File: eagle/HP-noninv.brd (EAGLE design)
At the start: 40.7 x 40.7 mm, 20 parts, among them IC1 OPA2134, IC2 TLE2426CLP

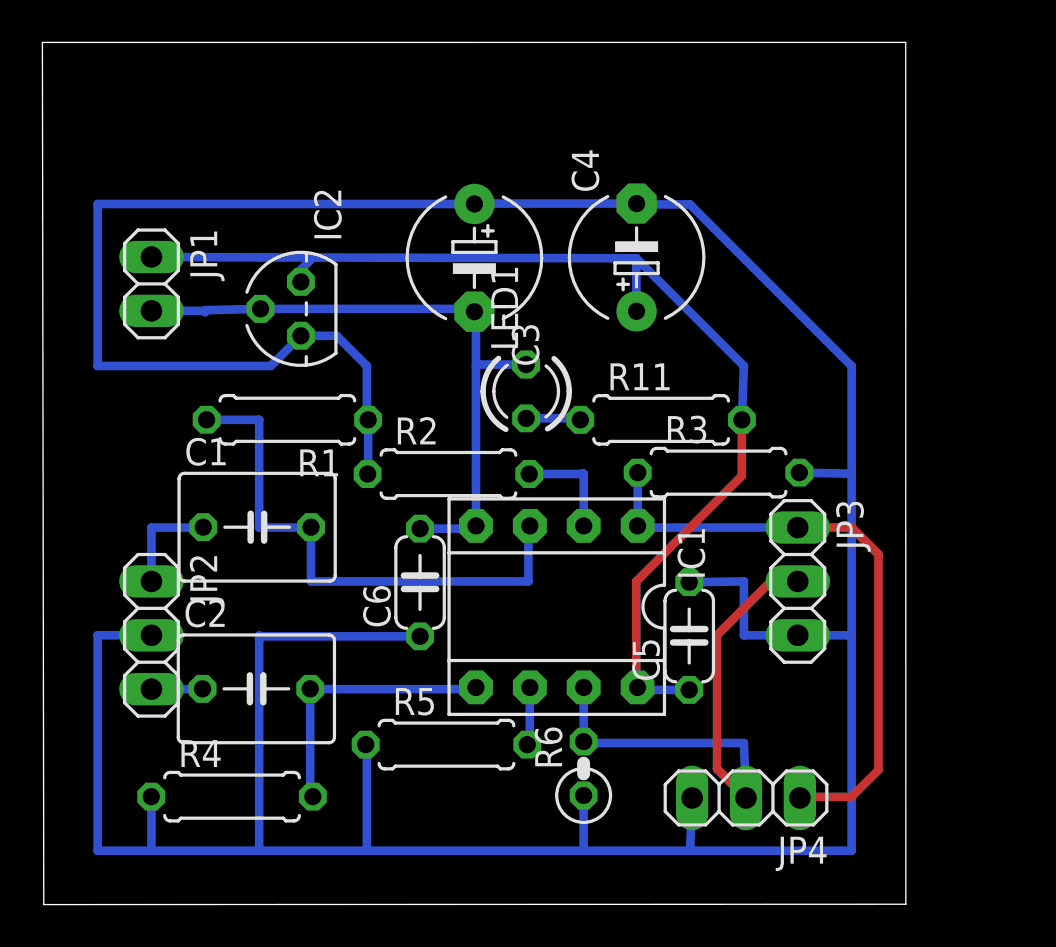
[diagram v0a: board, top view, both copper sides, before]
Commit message: 保護抵抗追加
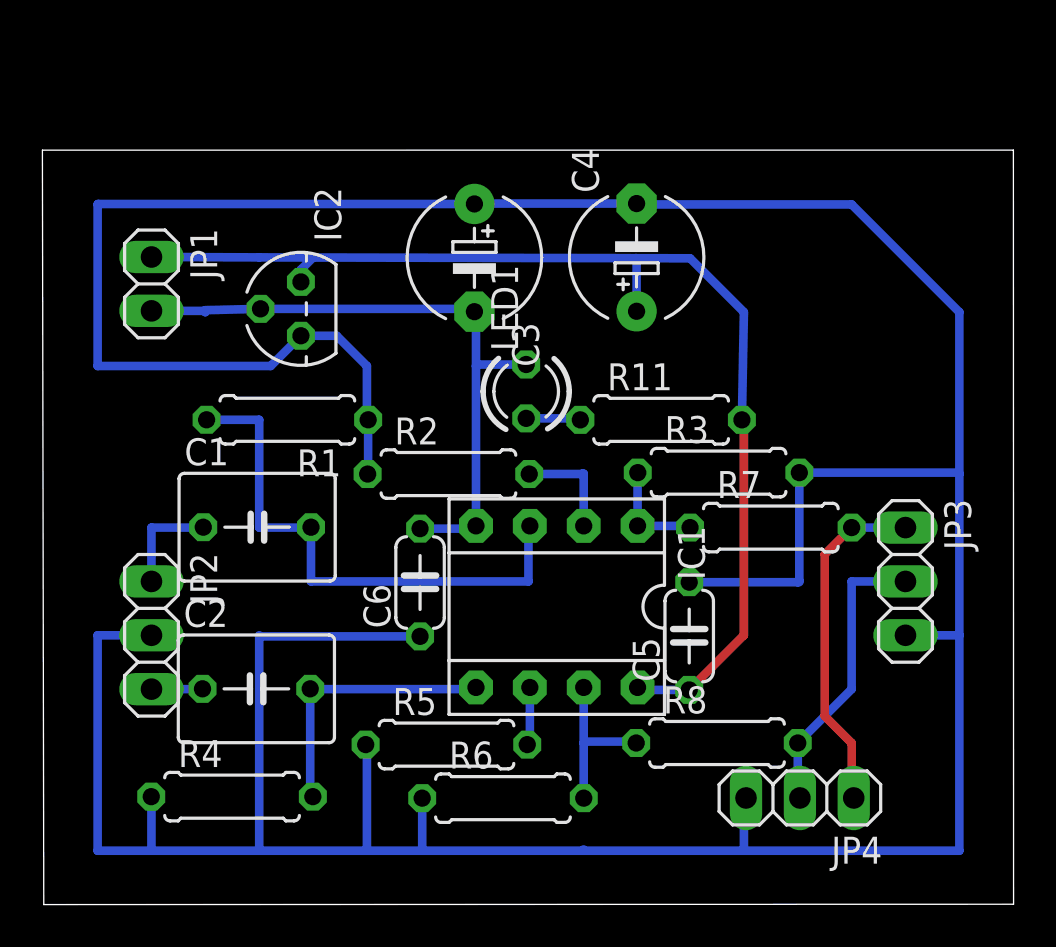
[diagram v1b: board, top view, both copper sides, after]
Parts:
- added R7, R8: (no value), rcl:0207/7
- R6: device rcl:0207/2V -> rcl:0207/7
- moved JP3 5.08 mm to (40.6, 15.2)
- moved R6 4.05 mm to (21.7, 5.02), turned to 0 degrees
- moved JP4 2.54 mm to (35.7, 5.03)
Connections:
- new net N$2: IC1.1, R3.1, R7.1
- new net N$4: IC1.7, R6.2, R8.1
- net N$11: now also R8.2; no longer IC1.7, R6.2
- net N$8: now also R7.2; no longer IC1.1, R3.1
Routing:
- net GND: track 179.7 -> 199.2 mm
- net N$8: track 28.9 -> 16.4 mm
- net N$11: track 26.0 -> 13.9 mm
- net N$4: track 0.00 -> 7.75 mm
- net N$2: track 0.00 -> 5.08 mm
- net VCC: track 53.7 -> 54.4 mm
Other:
- board size 40.7 x 40.7 mm -> 45.8 x 35.6 mm

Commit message: ケミコンを倒して配置
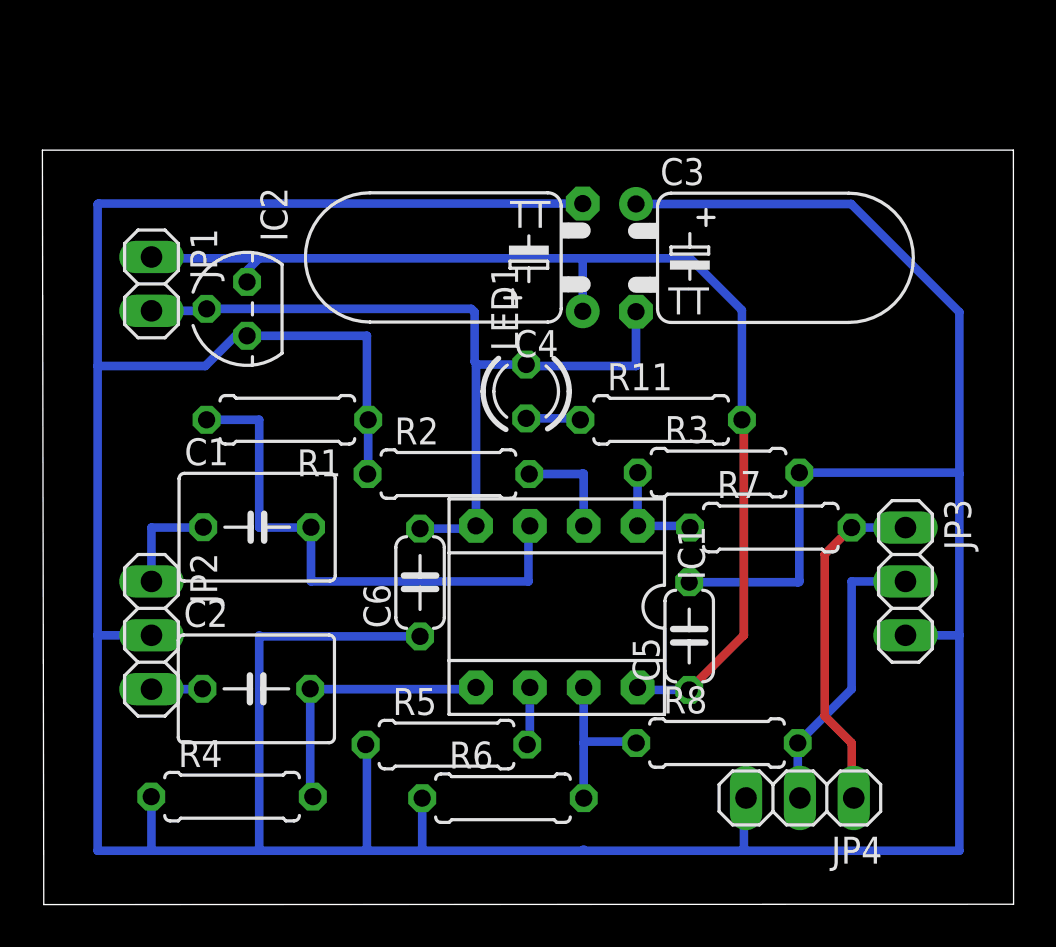
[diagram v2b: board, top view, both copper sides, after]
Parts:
- C3, C4: device rcl:E5-6 -> rcl:TT5D6L
- R11: value 1k -> 4.7k
- R7, R8: value (none) -> 22
- moved C3 7.62 mm to (27.9, 30.5)
- moved C4 2.54 mm to (25.4, 30.5)
- moved IC2 2.54 mm to (9.59, 28.1)
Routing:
- net GND: track 199.2 -> 210.2 mm
- net VEE: track 30.7 -> 38.5 mm
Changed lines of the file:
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@@
 <element name="R6" library="rcl" package="0207/7" value="47k" x="21.6567" y="5.019375"/>
 <element name="JP1" library="pinhead" package="1X02" value="PWR" x="5.080871875" y="29.271534375" rot="R270"/>
-<element name="R11" library="rcl" package="0207/7" value="1k" x="29.115325" y="22.860184375"/>
+<element name="R11" library="rcl" package="0207/7" value="4.7k" x="29.115325" y="22.860184375"/>
 <element name="LED1" library="led" package="LED3MM" value="Blue" x="22.75166875" y="24.200390625" rot="R90"/>
-<element name="IC2" library="tle2426" package="TO226AA" value="TLE2426CLP" x="12.1279375" y="28.09585" rot="R90"/>
-<element name="C3" library="rcl" package="E5-6" value="100u" x="20.310715625" y="30.502884375" rot="R270"/>
-<element name="C4" library="rcl" package="E5-6" value="100u" x="27.95845" y="30.520903125" rot="R90"/>
+<element name="IC2" library="tle2426" package="TO226AA" value="TLE2426CLP" x="9.5879375" y="28.09585" rot="R90"/>
+<element name="C3" library="rcl" package="TT5D6L" value="100u" x="27.930715625" y="30.502884375" rot="R270"/>
+<element name="C4" library="rcl" package="TT5D6L" value="100u" x="25.41845" y="30.520903125" rot="R90"/>
 <element name="C5" library="rcl" package="C050-024X044" value="0.1u" x="30.440721875" y="12.664484375" rot="R90"/>
 <element name="C6" library="rcl" package="C050-024X044" value="0.1u" x="17.74674375" y="15.189546875" rot="R90"/>
@@
 <element name="JP3" library="pinhead" package="1X03" value="OUTPUT1" x="40.64" y="15.24" rot="R270"/>
 <element name="JP4" library="pinhead" package="1X03" value="OUTPUT2" x="35.66021875" y="5.0287125" rot="R180"/>
-<element name="R7" library="rcl" package="0207/7" value="" x="34.29" y="17.78"/>
-<element name="R8" library="rcl" package="0207/7" value="" x="31.75" y="7.62"/>
+<element name="R7" library="rcl" package="0207/7" value="22" x="34.29" y="17.78"/>
+<element name="R8" library="rcl" package="0207/7" value="22" x="31.75" y="7.62"/>
 </elements>
 <signals>
@@
 <wire x1="15.182175" y1="7.54454375" x2="15.24" y2="7.54454375" width="0.4064" layer="16"/>
 <wire x1="15.24" y1="7.54454375" x2="15.24" y2="2.54" width="0.4064" layer="16"/>
-<wire x1="13.81415" y1="26.82585" x2="15.24" y2="25.4" width="0.4064" layer="16"/>
-<wire x1="15.24" y1="25.4" x2="15.24" y2="22.92230625" width="0.4064" layer="16"/>
+<wire x1="15.24" y1="26.82585" x2="15.24" y2="22.92230625" width="0.4064" layer="16"/>
 <wire x1="15.24" y1="22.92230625" x2="15.298746875" y2="22.863559375" width="0.4064" layer="16"/>
 <wire x1="15.298746875" y1="22.863559375" x2="15.298746875" y2="20.328196875" width="0.4064" layer="16"/>
 <wire x1="15.298746875" y1="20.328196875" x2="15.2750875" y2="20.3045375" width="0.4064" layer="16"/>
-<wire x1="27.95845" y1="33.060903125" x2="20.328734375" y2="33.060903125" width="0.4064" layer="16"/>
-<wire x1="20.328734375" y1="33.060903125" x2="20.310715625" y2="33.042884375" width="0.4064" layer="16"/>
 <contactref element="JP2" pad="2"/>
 <wire x1="5.08" y1="12.7" x2="2.54" y2="12.7" width="0.4064" layer="16"/>
 <wire x1="2.54" y1="12.7" x2="2.54" y2="2.54" width="0.4064" layer="16"/>
 <wire x1="2.54" y1="2.54" x2="5.08" y2="2.54" width="0.4064" layer="16"/>
-<wire x1="12.1279375" y1="26.82585" x2="10.7020875" y2="25.4" width="0.4064" layer="16"/>
-<wire x1="10.7020875" y1="25.4" x2="2.54" y2="25.4" width="0.4064" layer="16"/>
-<wire x1="2.54" y1="25.4" x2="2.54" y2="33.02" width="0.4064" layer="16"/>
-<wire x1="2.54" y1="33.02" x2="2.562884375" y2="33.042884375" width="0.4064" layer="16"/>
-<wire x1="2.562884375" y1="33.042884375" x2="20.310715625" y2="33.042884375" width="0.4064" layer="16"/>
-<wire x1="12.1279375" y1="26.82585" x2="13.81415" y2="26.82585" width="0.4064" layer="16"/>
+<wire x1="2.54" y1="33.02" x2="2.580903125" y2="33.060903125" width="0.4064" layer="16"/>
 <wire x1="43.18" y1="2.54" x2="33.02" y2="2.54" width="0.4064" layer="16"/>
 <wire x1="33.02" y1="2.54" x2="25.4" y2="2.54" width="0.4064" layer="16"/>
-<wire x1="43.18" y1="27.94" x2="38.1" y2="33.02" width="0.4064" layer="16"/>
-<wire x1="38.1" y1="33.02" x2="27.94" y2="33.02" width="0.4064" layer="16"/>
-<wire x1="27.94" y1="33.02" x2="27.95845" y2="33.060903125" width="0.4064" layer="16"/>
+<wire x1="43.18" y1="27.94" x2="38.077115625" y2="33.042884375" width="0.4064" layer="16"/>
 <contactref element="R6" pad="1"/>
 <wire x1="25.460625" y1="2.600625" x2="25.4" y2="2.54" width="0.4064" layer="16"/>
@@
 <wire x1="17.8467" y1="5.019375" x2="17.8467" y2="2.6067" width="0.4064" layer="16"/>
 <wire x1="17.8467" y1="2.6067" x2="17.78" y2="2.54" width="0.4064" layer="16"/>
+<wire x1="2.54" y1="33.02" x2="2.54" y2="25.4" width="0.4064" layer="16"/>
+<wire x1="2.54" y1="25.4" x2="2.54" y2="12.7" width="0.4064" layer="16"/>
+<wire x1="9.5879375" y1="26.82585" x2="9.04585" y2="26.82585" width="0.4064" layer="16"/>
+<wire x1="9.04585" y1="26.82585" x2="7.62" y2="25.4" width="0.4064" layer="16"/>
+<wire x1="7.62" y1="25.4" x2="2.54" y2="25.4" width="0.4064" layer="16"/>
+<wire x1="25.41845" y1="33.060903125" x2="2.580903125" y2="33.060903125" width="0.4064" layer="16"/>
+<wire x1="38.077115625" y1="33.042884375" x2="27.930715625" y2="33.042884375" width="0.4064" layer="16"/>
+<wire x1="9.5879375" y1="26.82585" x2="15.24" y2="26.82585" width="0.4064" layer="16"/>
 </signal>
 <signal name="N$5">
@@
 <wire x1="20.38411875" y1="17.729546875" x2="17.74674375" y2="17.729546875" width="0.4064" layer="16"/>
 <wire x1="20.38411875" y1="17.86044375" x2="20.38411875" y2="25.4" width="0.4064" layer="16"/>
-<wire x1="20.38411875" y1="25.4" x2="20.38411875" y2="27.88948125" width="0.4064" layer="16"/>
-<wire x1="20.38411875" y1="27.88948125" x2="20.310715625" y2="27.962884375" width="0.4064" layer="16"/>
 <wire x1="22.75166875" y1="25.470390625" x2="20.454509375" y2="25.470390625" width="0.4064" layer="16"/>
 <wire x1="20.454509375" y1="25.470390625" x2="20.38411875" y2="25.4" width="0.4064" layer="16"/>
@@
 <wire x1="7.558465625" y1="28.001534375" x2="7.62" y2="27.94" width="0.4064" layer="16"/>
 <wire x1="7.62" y1="27.94" x2="7.62" y2="28.0329125" width="0.4064" layer="16"/>
-<wire x1="7.62" y1="28.0329125" x2="10.2229375" y2="28.09585" width="0.4064" layer="16"/>
-<wire x1="10.2229375" y1="28.09585" x2="20.17775" y2="28.09585" width="0.4064" layer="16"/>
-<wire x1="20.17775" y1="28.09585" x2="20.310715625" y2="27.962884375" width="0.4064" layer="16"/>
+<wire x1="7.62" y1="28.0329125" x2="7.6829375" y2="28.09585" width="0.4064" layer="16"/>
+<wire x1="7.6829375" y1="28.09585" x2="20.16415" y2="28.09585" width="0.4064" layer="16"/>
+<wire x1="20.16415" y1="28.09585" x2="20.32" y2="27.94" width="0.4064" layer="16"/>
+<wire x1="20.32" y1="27.94" x2="20.32" y2="25.6049" width="0.4064" layer="16"/>
+<wire x1="20.32" y1="25.6049" x2="20.454509375" y2="25.470390625" width="0.4064" layer="16"/>
+<wire x1="27.930715625" y1="27.962884375" x2="27.930715625" y2="25.409284375" width="0.4064" layer="16"/>
+<wire x1="27.930715625" y1="25.409284375" x2="27.94" y2="25.4" width="0.4064" layer="16"/>
+<wire x1="27.94" y1="25.4" x2="22.822059375" y2="25.4" width="0.4064" layer="16"/>
+<wire x1="22.822059375" y1="25.4" x2="22.75166875" y2="25.470390625" width="0.4064" layer="16"/>
 </signal>
 <signal name="VCC">
@@
 <wire x1="28.00411875" y1="10.24044375" x2="28.00411875" y2="10.124484375" width="0.4064" layer="16"/>
 <wire x1="28.00411875" y1="10.124484375" x2="30.440721875" y2="10.124484375" width="0.4064" layer="16"/>
-<wire x1="5.080871875" y1="30.541534375" x2="10.160103125" y2="30.523075" width="0.4064" layer="16"/>
-<wire x1="10.160103125" y1="30.523075" x2="12.700090625" y2="30.516921875" width="0.4064" layer="16"/>
-<wire x1="12.700090625" y1="30.516921875" x2="27.9400125" y2="30.485275" width="0.4064" layer="16"/>
-<wire x1="27.9400125" y1="30.485275" x2="30.48" y2="30.48" width="0.4064" layer="16"/>
-<wire x1="30.48" y1="30.48" x2="33.02" y2="27.94" width="0.4064" layer="16"/>
-<wire x1="33.02" y1="27.94" x2="32.925325" y2="22.860184375" width="0.4064" layer="16"/>
-<wire x1="12.1279375" y1="29.36585" x2="12.1279375" y2="29.94476875" width="0.4064" layer="16"/>
-<wire x1="12.1279375" y1="29.94476875" x2="12.700090625" y2="30.516921875" width="0.4064" layer="16"/>
-<wire x1="27.95845" y1="27.980903125" x2="27.95845" y2="30.4668375" width="0.4064" layer="16"/>
-<wire x1="27.95845" y1="30.4668375" x2="27.9400125" y2="30.485275" width="0.4064" layer="16"/>
 <wire x1="30.440721875" y1="10.124484375" x2="30.444484375" y2="10.124484375" width="0.4064" layer="1"/>
 <wire x1="30.444484375" y1="10.124484375" x2="33.02" y2="12.7" width="0.4064" layer="1"/>
 <wire x1="33.02" y1="12.7" x2="33.02" y2="22.765509375" width="0.4064" layer="1"/>
 <wire x1="33.02" y1="22.765509375" x2="32.925325" y2="22.860184375" width="0.4064" layer="1"/>
+<wire x1="32.925325" y1="22.860184375" x2="32.925325" y2="28.034675" width="0.4064" layer="16"/>
+<wire x1="32.925325" y1="28.034675" x2="30.48" y2="30.48" width="0.4064" layer="16"/>
+<wire x1="30.48" y1="30.48" x2="25.4" y2="30.48" width="0.4064" layer="16"/>
+<wire x1="25.4" y1="30.48" x2="10.16" y2="30.48" width="0.4064" layer="16"/>
+<wire x1="10.16" y1="30.48" x2="5.14240625" y2="30.48" width="0.4064" layer="16"/>
+<wire x1="5.14240625" y1="30.48" x2="5.080871875" y2="30.541534375" width="0.4064" layer="16"/>
+<wire x1="9.5879375" y1="29.36585" x2="9.5879375" y2="29.9079375" width="0.4064" layer="16"/>
+<wire x1="9.5879375" y1="29.9079375" x2="10.16" y2="30.48" width="0.4064" layer="16"/>
+<wire x1="25.41845" y1="27.980903125" x2="25.41845" y2="30.46155" width="0.4064" layer="16"/>
+<wire x1="25.41845" y1="30.46155" x2="25.4" y2="30.48" width="0.4064" layer="16"/>
 </signal>
 <signal name="N$9">

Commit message: 積セラの配置を変更
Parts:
- C5: device rcl:C050-024X044 -> rcl:C025-024X044
- R2, R5: value 22k -> 12k
- moved JP3 8.03 mm to (38.1, 7.62)
- moved JP4 5.76 mm to (40.8, 7.64), turned to 270 degrees
- moved C5 1.27 mm to (30.4, 11.4)
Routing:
- net N$11: track 13.9 -> 5.26 mm
- net N$8: track 16.4 -> 10.3 mm
- net VCC: track 54.3 -> 58.3 mm
- net GND: track 210.2 -> 212.9 mm

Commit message: Hardware完成
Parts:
- moved R3 2.69 mm to (29.1, 20.3), turned to 180 degrees
- moved R2 0.08 mm to (19.0, 20.3), turned to 180 degrees
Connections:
- net GND: now also R2.2; no longer R2.1, R3.2, R6.1
- net N$7: now also R2.1, R3.2; no longer R2.2
- net N$9: now also R6.1
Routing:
- net GND: track 212.9 -> 202.8 mm
- net N$9: track 2.82 -> 10.4 mm
- net VCC: track 58.3 -> 61.9 mm
- net N$2: track 5.08 -> 6.09 mm
